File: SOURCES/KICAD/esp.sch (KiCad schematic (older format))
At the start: 19 parts, among them IC501 ESP32-WROOM-32U, IC502 IC_NCP1117LPST33, Q501 Q_SS8050-G, Q502 Q_SS8050-G, SW501 SW_Push, X501 Conn_01x04, X502 Conn_01x05, X503 Conn_01x03, X504 HDR_01x06

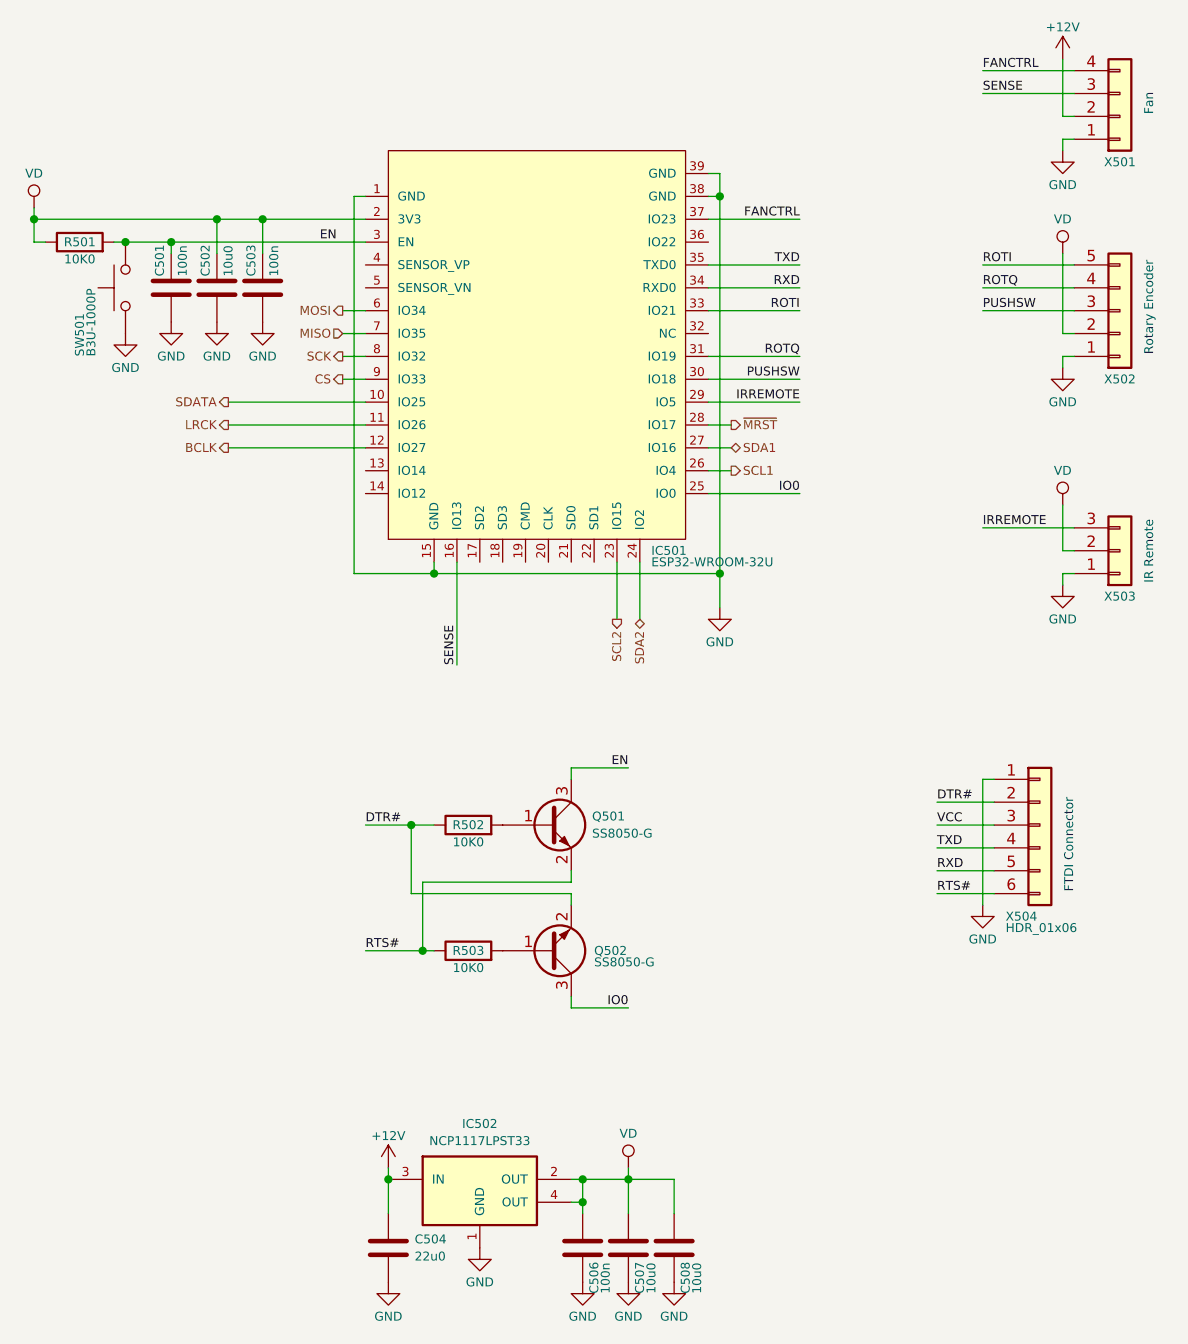
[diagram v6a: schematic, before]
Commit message: Bugfix: Made WiFi pins unconnected
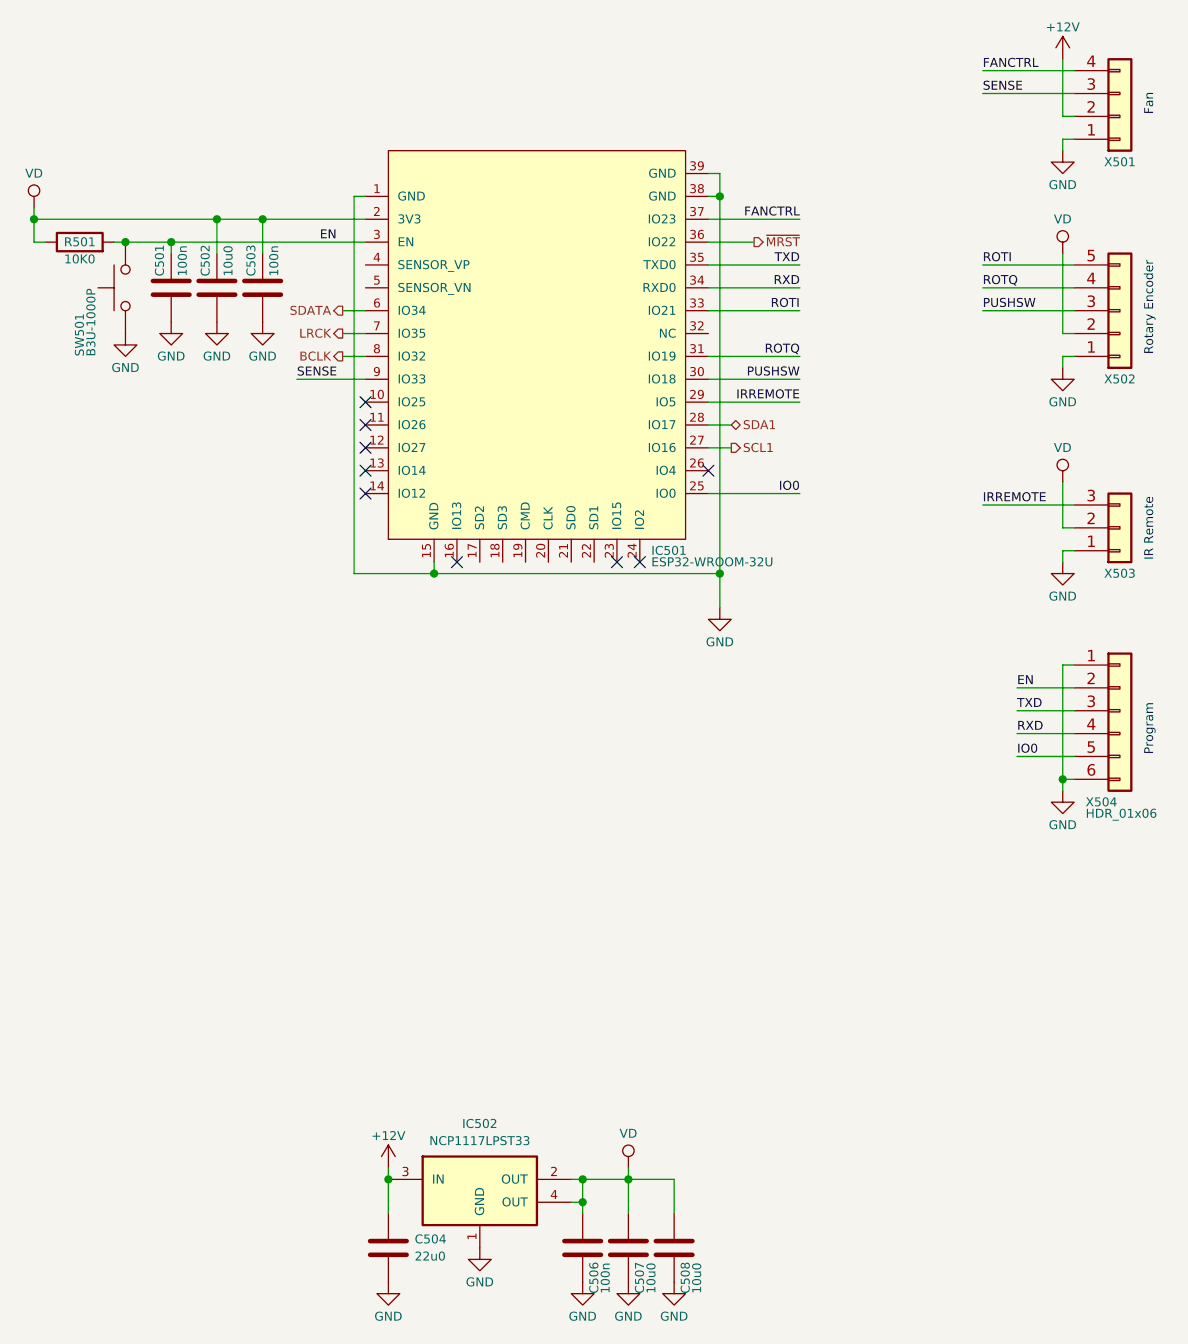
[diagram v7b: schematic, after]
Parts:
- removed Q501, Q502: Q_SS8050-G, Package_TO_SOT_SMD:SOT-23, symbol Device:Q_NPN_BEC
- removed R502, R503: RES_10K0_1%_0.125W_Thick_0805, rklib:C0805-RES, symbol rk:RES_10K0_1%_0.125W_Thick_0805
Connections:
- net CS is gone; now on net SENSE: IC501.9 (IO33)
- net DTR# is gone; now on net EN: X504.2 (Pin_2)
- net MISO is gone; now on net LRCK: IC501.7 (IO35)
- net MOSI is gone; now on net SDATA: IC501.6 (IO34)
- net RTS# is gone; now on net GND: X504.6 (Pin_6)
- net SCK is gone; now on net BCLK: IC501.8 (IO32)
- net VCC is gone; now on net TXD: X504.3 (Pin_3)
- net BCLK: no longer IC501.12 (IO27)
- net IO0: now also X504.5 (Pin_5)
- net LRCK: no longer IC501.11 (IO26)
- net RXD: now also X504.4 (Pin_4); no longer X504.5 (Pin_5)
- net SCL1: now also IC501.27 (IO16); no longer IC501.26 (IO4)
- net SDA1: now also IC501.28 (IO17); no longer IC501.27 (IO16)
- net SDATA: no longer IC501.10 (IO25)
- net SENSE: no longer IC501.16 (IO13)
- net TXD: no longer X504.4 (Pin_4)
- net ~MRST: now also IC501.36 (IO22); no longer IC501.28 (IO17)
- net SCL2: no longer names the net of IC501.23 (IO15)
- net SDA2: no longer names the net of IC501.24 (IO2)
- no-connect marks 0 -> 9
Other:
- note added: "Program"
- note removed: "FTDI Connector"
- moved on the sheet: X503, X504
